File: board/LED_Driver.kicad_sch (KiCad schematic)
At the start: 10 parts, among them J4 Conn_01x04, Q1 BSC028N06LS3, Q2 BSC028N06LS3, Q3 BSC028N06LS3

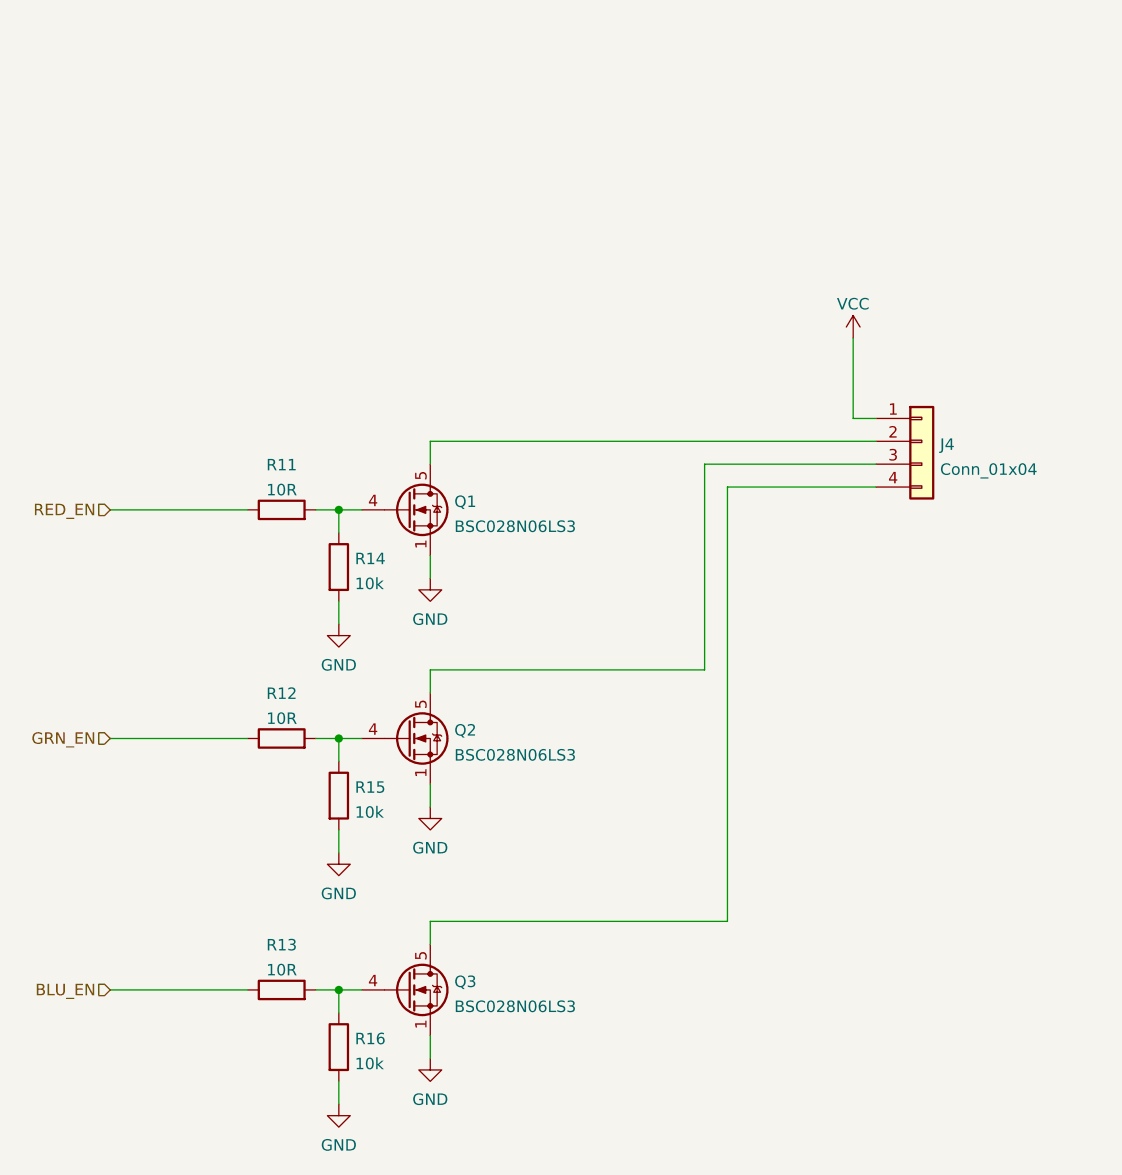
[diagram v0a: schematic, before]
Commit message: doing some cost reduction
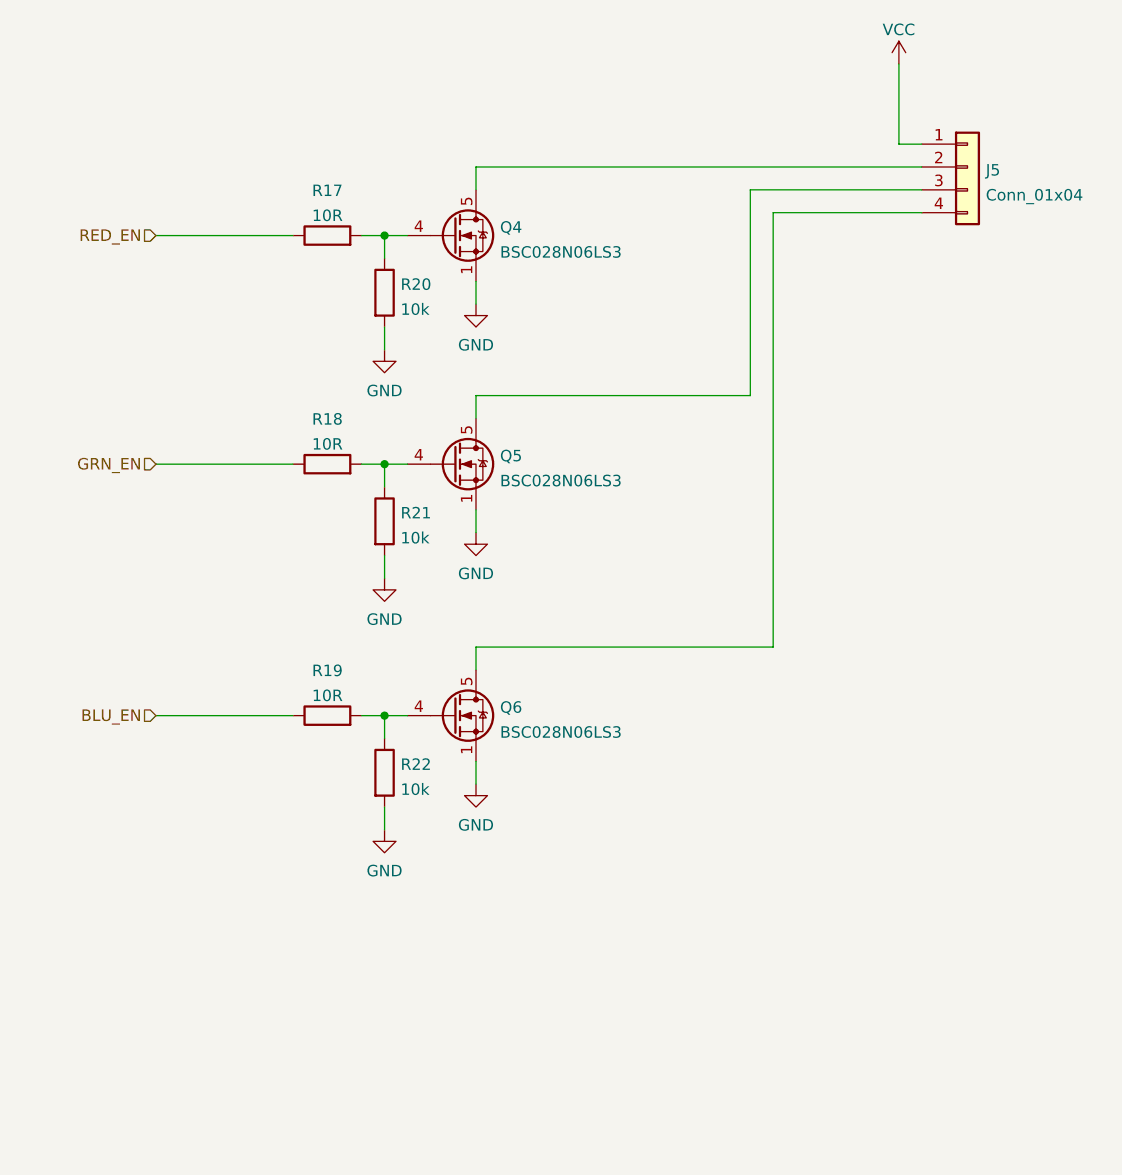
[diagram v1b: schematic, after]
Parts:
- renumbered J4 to J5, Q1 to Q4, Q2 to Q5, Q3 to Q6, R11 to R17, R12 to R18, R13 to R19, R14 to R20, R15 to R21, R16 to R22
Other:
- moved on the sheet: J5, Q4, Q5, Q6, R17, R18, R19, R20, R21, R22
